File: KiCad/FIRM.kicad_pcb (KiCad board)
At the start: 4 copper layers, 95 parts, among them J1 Conn_01x02_Pin, J3 Micro_SD_Card_Det2, J5 USB_C_Receptacle_USB2.0_16P, Q2 IRLML6402, SW1 PTS815, U1 STM32F405RGTx, U2 MIC5219-3.3YM5, U7 W25Q128JVS, X2 32.768khz, Y1 12mhz

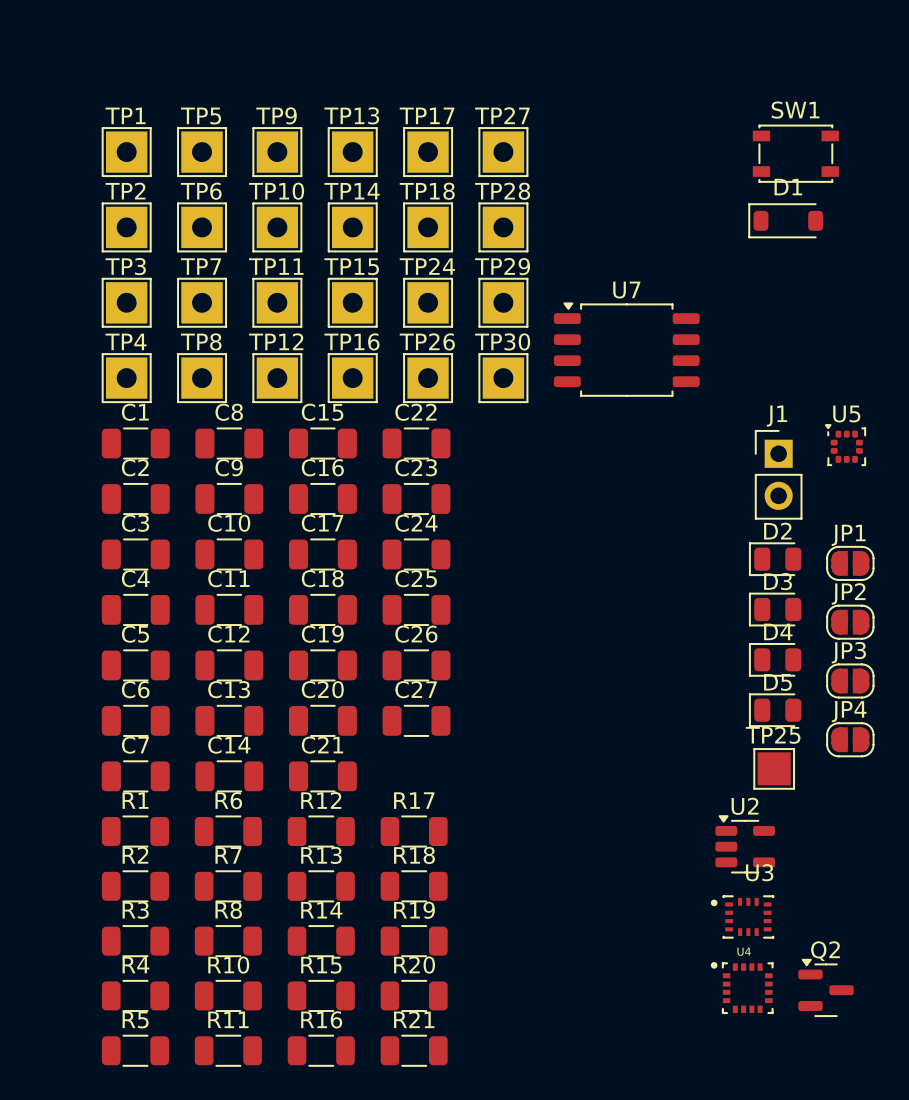
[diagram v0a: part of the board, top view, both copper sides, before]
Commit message: changing some sizes
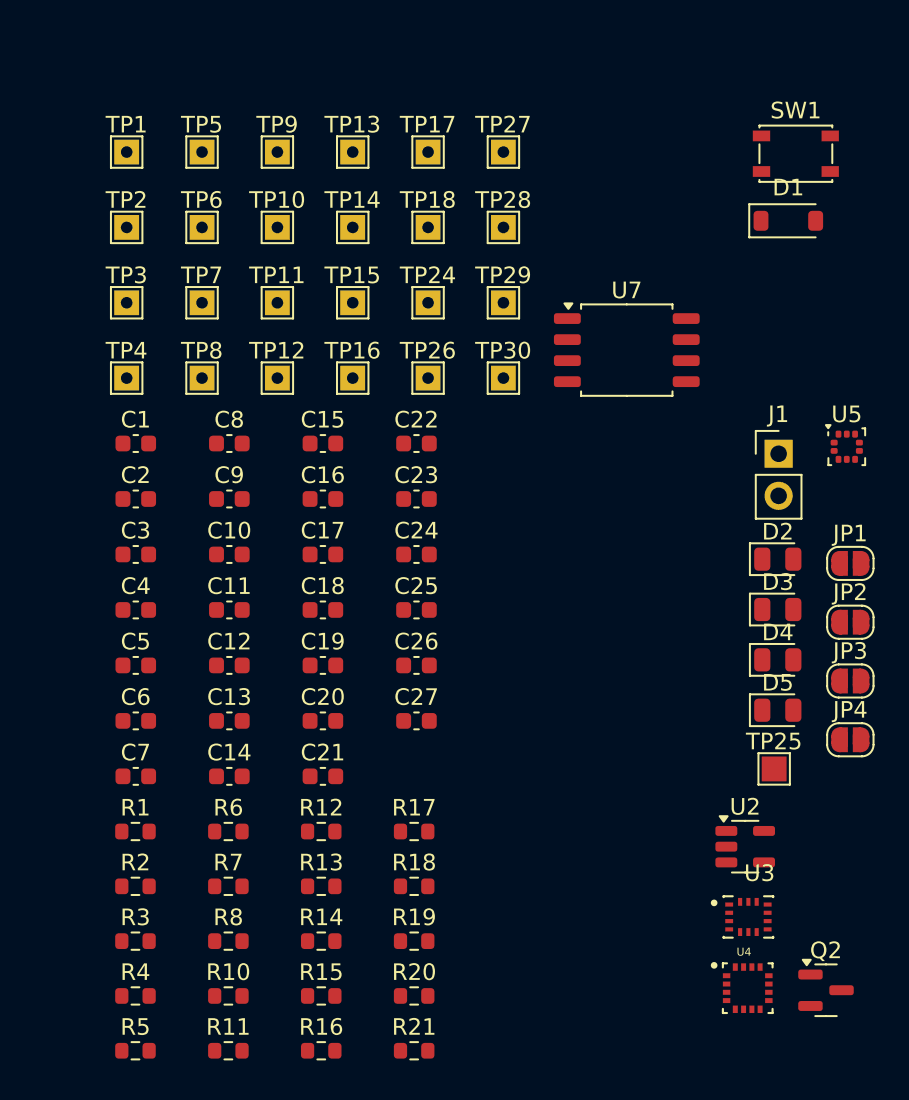
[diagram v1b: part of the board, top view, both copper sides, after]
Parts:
- C1, C10, C11, C12, C13, C14, C15, C16, C17, C18, C19, C2, C20, C21, C22, C23, C24, C25, C26, C27, C3, C4, C5, C6, C7, C8, C9: footprint Capacitor_SMD:C_1206_3216Metric -> Capacitor_SMD:C_0603_1608Metric
- R1, R10, R11, R12, R13, R14, R15, R16, R17, R18, R19, R2, R20, R21, R3, R4, R5, R6, R7, R8: footprint Resistor_SMD:R_1206_3216Metric -> Resistor_SMD:R_0603_1608Metric
- TP1, TP10, TP11, TP12, TP13, TP14, TP15, TP16, TP17, TP18, TP2, TP24, TP26, TP27, TP28, TP29, TP3, TP30, TP4, TP5, TP6, TP7, TP8, TP9: footprint TestPoint:TestPoint_THTPad_2.5x2.5mm_Drill1.2mm -> TestPoint:TestPoint_THTPad_1.5x1.5mm_Drill0.7mm
- TP25: footprint TestPoint:TestPoint_Pad_2.0x2.0mm -> TestPoint:TestPoint_Pad_1.5x1.5mm

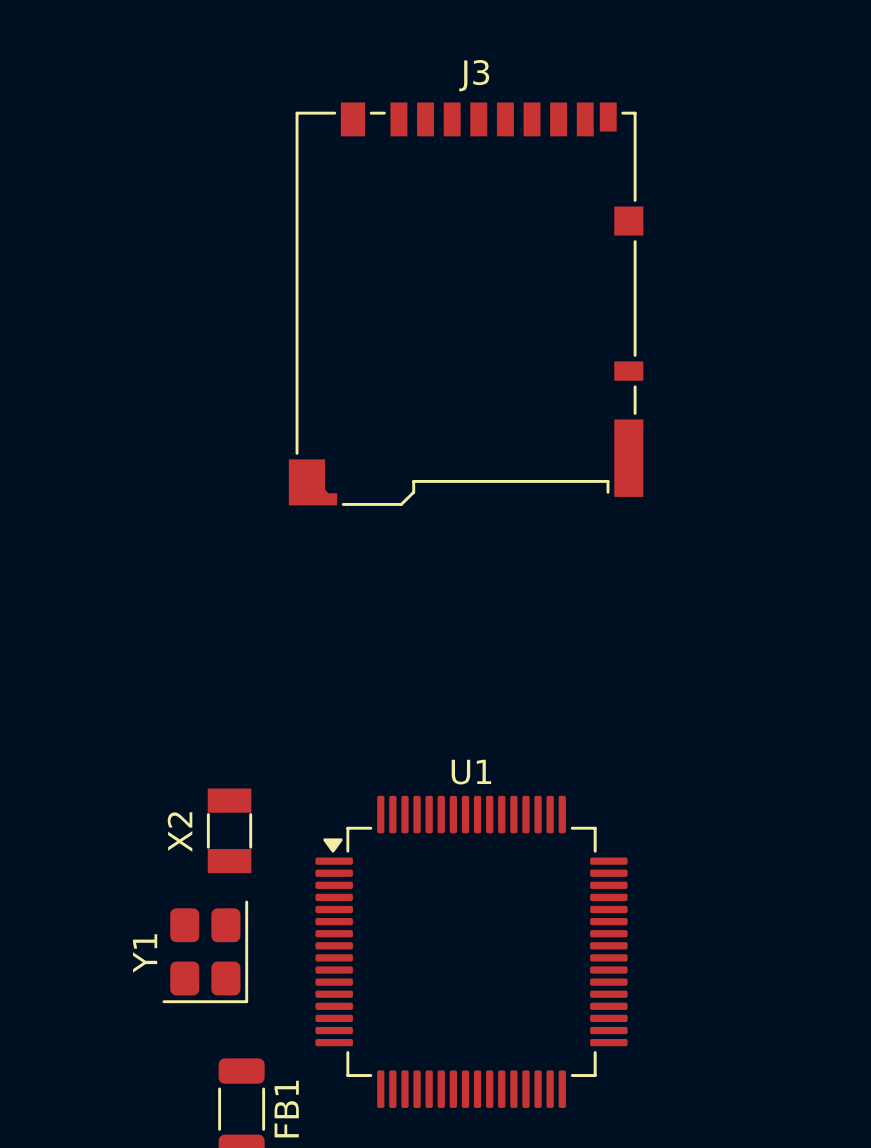
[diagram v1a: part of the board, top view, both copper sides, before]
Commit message: update crystal and sd card port
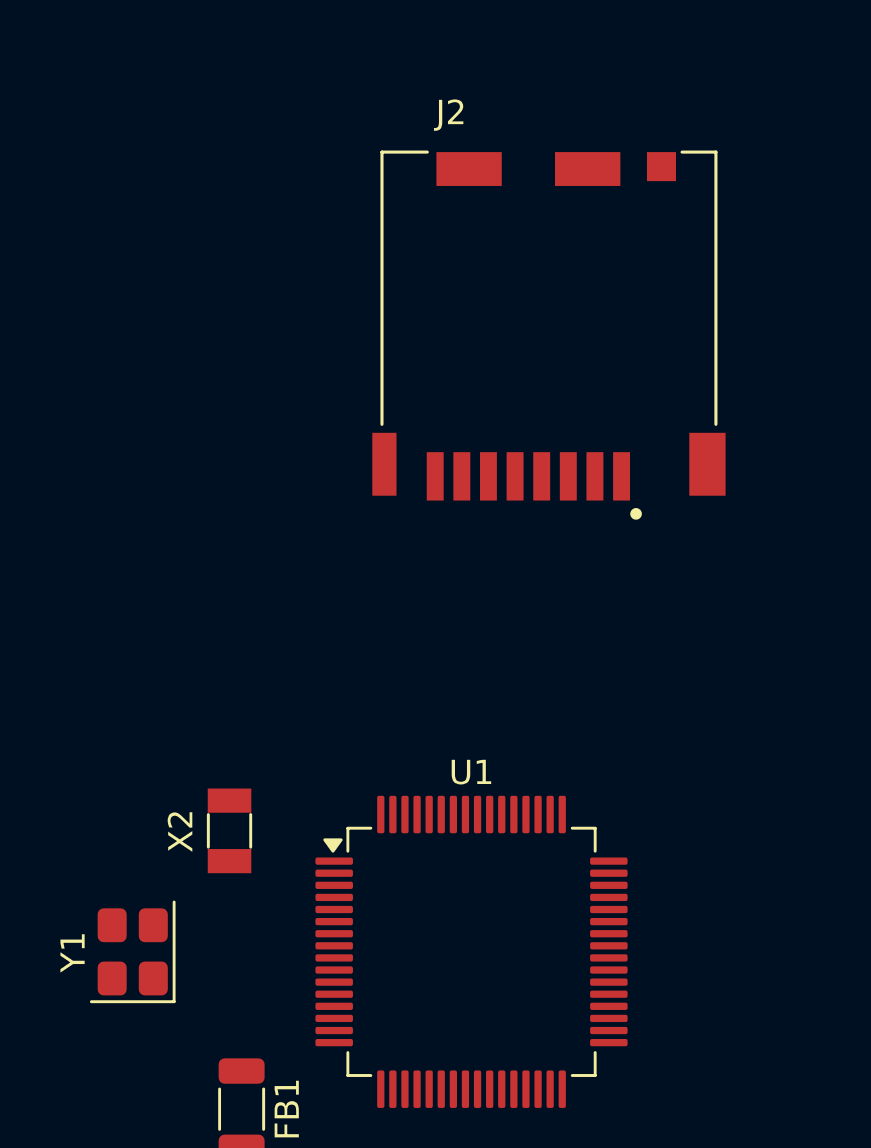
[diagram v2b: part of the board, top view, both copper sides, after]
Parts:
- removed J3: Micro_SD_Card_Det2, Connector_Card:microSD_HC_Hirose_DM3BT-DSF-PEJS
- added J2: DM3CS-SF, DM3CS-SF:HRS_DM3CS-SF, F.Cu at (136.5, 53.5)
- Y1: value 12mhz -> 12 MHz; footprint Crystal:Crystal_SMD_3225-4Pin_3.2x2.5mm -> Crystal:Crystal_SMD_Abracon_ABM8G-4Pin_3.2x2.5mm
- moved Y1 3.00 mm to (119.5, 79.5)
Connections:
- Y1 pad 1: /HSE_OUT -> /HSE_IN
- Y1 pad 2: /HSE_IN -> GND
- Y1 pad 3: (no net) -> /HSE_OUT
- Y1 pad 4: (no net) -> GND

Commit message: rough layout
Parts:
- JP1, JP2, JP3, JP4, U7: moved to B.Cu
- moved J1 99.9 mm to (111.0, 105.5)
- moved U4 97.5 mm to (146.0, 59.5)
- moved TP25 97.1 mm to (132.5, 63.0)
- moved Q2 96.6 mm to (121.0, 107.0), turned to 180 degrees
- moved D5 95.2 mm to (116.5, 104.0), turned to 90 degrees
- moved R5 94.3 mm to (136.3, 50.5), turned to 180 degrees
- moved SW1 93.5 mm to (120.5, 63.5), turned to -90 degrees
- moved JP4 92.0 mm to (151.7, 52.5)
- moved R7 90.7 mm to (135.5, 47.5), turned to 180 degrees
- moved R6 89.2 mm to (117.0, 59.0), turned to -90 degrees
- moved R4 88.9 mm to (136.3, 53.0), turned to 180 degrees
- moved R20 88.9 mm to (136.0, 63.0), turned to -90 degrees
- moved D1 87.1 mm to (126.5, 107.0), turned to -90 degrees
- moved JP3 87.0 mm to (151.7, 56.0)
- moved TP30 86.4 mm to (111.0, 73.8), turned to -90 degrees
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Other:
- board outline added: 57.5 x 70.3 mm

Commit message: Use project library instead of global library
Also reorganize footprints, custom symbols, and 3d models. Updated README about using KiCad in the project.
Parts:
- U3: footprint ICM-45686:IC_ICM-45686 -> sensors:IC_ICM-45686
- U4: footprint MMC5983MA:PQFN50P300X300X100-16N -> sensors:IC_MMC5983MA
- U5: footprint Package_LGA:ST_HLGA-10_2x2mm_P0.5mm_LayoutBorder3x2y -> sensors:BMP581
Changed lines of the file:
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@@
 		(embedded_fonts no)
 	)
-	(footprint "ICM-45686:IC_ICM-45686"
+	(footprint "sensors:IC_ICM-45686"
 		(layer "F.Cu")
 		(at 151.5 99.5)
@@
 		)
 		(embedded_fonts no)
+		(model "${KIPRJMOD}/3dmodels/ICM-45686.step"
+			(offset
+				(xyz 0 0 0)
+			)
+			(scale
+				(xyz 1 1 1)
+			)
+			(rotate
+				(xyz -90 -0 -0)
+			)
+		)
 	)
 	(footprint "TestPoint:TestPoint_THTPad_1.5x1.5mm_Drill0.7mm"
@@
 		)
 	)
-	(footprint "Package_LGA:ST_HLGA-10_2x2mm_P0.5mm_LayoutBorder3x2y"
+	(footprint "sensors:BMP581"
 		(layer "F.Cu")
 		(at 145 93.5)
@@
 		)
 		(embedded_fonts no)
-		(model "${KICAD9_3DMODEL_DIR}/Package_LGA.3dshapes/ST_HLGA-10_2x2mm_P0.5mm_LayoutBorder3x2y.step"
+		(model "${KIPRJMOD}/3dmodels/BMP581.step"
 			(offset
 				(xyz 0 0 0)
@@
 			)
 			(rotate
-				(xyz 0 0 0)
+				(xyz -90 -0 -0)
 			)
 		)
@@
 		)
 	)
-	(footprint "MMC5983MA:PQFN50P300X300X100-16N"
+	(footprint "sensors:IC_MMC5983MA"
 		(layer "F.Cu")
 		(at 146 59.5)
@@
 				(font
 					(size 0.48 0.48)
-					(thickness 0.15)
+					(thickness 0.12)
 				)
 			)
@@
 				(font
 					(size 0.48 0.48)
-					(thickness 0.15)
+					(thickness 0.12)
 				)
 			)
@@
 		)
 		(embedded_fonts no)
+		(model "${KIPRJMOD}/3dmodels/MMC5983MA.step"
+			(offset
+				(xyz 0 0 0)
+			)
+			(scale
+				(xyz 1 1 1)
+			)
+			(rotate
+				(xyz -90 -0 -0)
+			)
+		)
 	)
 	(footprint "Resistor_SMD:R_0603_1608Metric"

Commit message: im firm
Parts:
- removed J5: USB_C_Receptacle_USB2.0_16P, Connector_USB:USB_C_Receptacle_Amphenol_124019772112A
- removed R16, R17: 5.1k, Resistor_SMD:R_0603_1608Metric
- added H1: MountingHole_Pad, MountingHole:MountingHole_3.2mm_M3_Pad_Via, F.Cu at (113.2, 130.5)
- added H2: MountingHole_Pad, MountingHole:MountingHole_3.2mm_M3_Pad_Via, F.Cu at (130.5, 100.0)
- added H3: MountingHole_Pad, MountingHole:MountingHole_3.2mm_M3_Pad_Via, F.Cu at (100.0, 100.0)
- added R22: 5.1k, Resistor_SMD:R_0603_1608Metric, F.Cu at (124.0, 133.2)
- added R9: 5.1k, Resistor_SMD:R_0603_1608Metric, F.Cu at (123.1, 131.6)
- added U6: A-USBC-20F0-EA-GSR05, connectors:A-USBC-20F0-EA-GSR05, F.Cu at (125.0, 125.5)
- J2, TP25: moved to B.Cu
- moved TP27 93.1 mm to (97.5, 127.5)
- moved TP17 88.6 mm to (105.2, 132.6)
- moved TP9 83.4 mm to (102.6, 132.6)
- moved JP2 82.8 mm to (105.0, 128.0), turned to -90 degrees
- moved JP4 82.7 mm to (105.8, 121.2)
- moved JP3 82.2 mm to (105.8, 124.2)
- moved JP1 81.6 mm to (101.5, 128.0), turned to -90 degrees
- moved TP8 77.8 mm to (100.1, 132.6)
- moved U4 76.7 mm to (101.5, 122.0), turned to 90 degrees
- moved TP28 76.5 mm to (97.5, 130.0)
- moved TP5 75.8 mm to (97.5, 119.9)
- moved C18 75.7 mm to (102.1, 124.8), turned to 0 degrees
- moved C17 69.4 mm to (100.7, 118.4), turned to 0 degrees
- moved TP4 67.7 mm to (97.5, 117.3), turned to 90 degrees
- moved TP18 67.2 mm to (107.7, 132.6)
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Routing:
- net GND: track 0.00 -> 60.7 mm, vias 0 -> 55
- net /I2C1_SDA: track 0.00 -> 49.9 mm, vias 0 -> 1
- net /PB4: track 0.00 -> 47.0 mm, vias 0 -> 2
- net /BOOT0: track 0.00 -> 46.8 mm, vias 0 -> 2
- net /I2C1_SCL: track 0.00 -> 45.8 mm, vias 0 -> 5
- net /MOSI2: track 0.00 -> 45.6 mm, vias 0 -> 4
- net VBUS: track 0.00 -> 44.7 mm
- net /PB5: track 0.00 -> 42.8 mm, vias 0 -> 4
- net /MISO2: track 0.00 -> 41.9 mm, vias 0 -> 4
- net Net-(D2-A): track 0.00 -> 41.3 mm, vias 0 -> 4
- net /SDIO_D2: track 0.00 -> 41.0 mm, vias 0 -> 3
- net /SDIO_D1: track 0.00 -> 40.5 mm, vias 0 -> 2
- net /SCK2: track 0.00 -> 40.5 mm, vias 0 -> 3
- net /SDIO_D3: track 0.00 -> 39.4 mm, vias 0 -> 4
- net /SDIO_CMD: track 0.00 -> 39.3 mm, vias 0 -> 6
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- added copper zone on In2.Cu, net +3.3V
- added copper zone on In1.Cu, net GND
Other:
- board size 57.5 x 70.3 mm -> 38.5 x 38.5 mm

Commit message: for the clanker
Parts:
- H1, H2, H3: footprint MountingHole:MountingHole_3.2mm_M3_Pad_Via -> MountingHole:MountingHole_2.2mm_M2_Pad_Via
- moved R6 74.0 mm to (180.2, 108.3), turned to 0 degrees
- moved R8 72.7 mm to (178.2, 125.5), turned to 0 degrees
- moved R5 70.3 mm to (179.7, 110.0), turned to 0 degrees
- moved C23 70.0 mm to (174.2, 121.3)
- moved Q2 68.9 mm to (171.2, 129.8), turned to -90 degrees
- moved R7 68.4 mm to (179.4, 111.5), turned to 180 degrees
- moved C22 68.0 mm to (168.0, 131.0)
- moved U2 67.8 mm to (171.2, 121.0), turned to 90 degrees
- moved C5 67.5 mm to (180.2, 104.5), turned to 0 degrees
- moved D1 66.2 mm to (173.7, 126.0), turned to 0 degrees
- moved D5 65.5 mm to (165.4, 126.3), turned to 0 degrees
- moved C9 64.8 mm to (181.9, 110.8), turned to 90 degrees
- moved C24 63.5 mm to (171.2, 118.0)
- moved R15 60.0 mm to (168.4, 126.0)
- moved C2 56.9 mm to (166.9, 100.0), turned to 0 degrees
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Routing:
- net GND: track 60.7 -> 4.16 mm, vias 55 -> 4
- net /I2C1_SDA: track 49.9 -> 1.83 mm, vias 1 -> 0
- net /PB4: track 47.0 -> 0.00 mm, vias 2 -> 0
- net /BOOT0: track 46.8 -> 0.00 mm, vias 2 -> 0
- net VBUS: track 44.7 -> 0.00 mm
- net /I2C1_SCL: track 45.8 -> 1.71 mm, vias 5 -> 0
- net /MOSI2: track 45.6 -> 2.21 mm, vias 4 -> 0
- net /PB5: track 42.8 -> 0.00 mm, vias 4 -> 0
- net Net-(D2-A): track 41.3 -> 0.00 mm, vias 4 -> 0
- net /SDIO_D2: track 41.0 -> 0.00 mm, vias 3 -> 0
- net /SDIO_D1: track 40.5 -> 0.00 mm, vias 2 -> 0
- net /SDIO_D3: track 39.4 -> 0.00 mm, vias 4 -> 0
- net /SDIO_CMD: track 39.3 -> 0.00 mm, vias 6 -> 0
- net /SCK2: track 40.5 -> 1.62 mm, vias 3 -> 0
- net /SDIO_CK: track 38.8 -> 0.00 mm, vias 3 -> 0
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
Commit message: bom digikey
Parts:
- TP25: moved to F.Cu
- U5: footprint sensors:BMP581 -> Package_LGA:ST_HLGA-10_2x2mm_P0.5mm_LayoutBorder3x2y
- moved R6 77.3 mm to (103.0, 104.5), turned to -90 degrees
- moved R7 73.3 mm to (106.3, 105.9), turned to 90 degrees
- moved R5 71.9 mm to (107.9, 104.4), turned to -90 degrees
- moved R18 71.2 mm to (103.0, 110.4), turned to 90 degrees
- moved R19 68.2 mm to (102.4, 107.2)
- moved C10 67.1 mm to (113.3, 100.0)
- moved R14 59.1 mm to (103.7, 115.9), turned to 90 degrees
- moved C27 58.4 mm to (105.1, 119.6)
- moved C23 58.2 mm to (116.2, 126.2), turned to 180 degrees
- moved C9 57.6 mm to (124.6, 104.5), turned to 0 degrees
- moved FB1 57.4 mm to (110.5, 119.7), turned to 180 degrees
- moved R21 57.4 mm to (105.2, 113.5), turned to 0 degrees
- moved C16 57.3 mm to (109.9, 123.5), turned to 0 degrees
- moved C11 57.2 mm to (104.8, 109.9), turned to 90 degrees
- moved C19 56.6 mm to (119.7, 120.3), turned to 0 degrees
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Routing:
- net /MOSI2: track 2.21 -> 83.3 mm, vias 0 -> 3
- net /MISO2: track 8.19 -> 85.0 mm, vias 2 -> 7
- net /SCK2: track 1.62 -> 74.8 mm, vias 0 -> 5
- net GND: track 4.16 -> 59.6 mm, vias 4 -> 61
- net /PA8: track 0.00 -> 54.1 mm, vias 0 -> 1
- net /PB10: track 0.00 -> 51.6 mm, vias 0 -> 2
- net /MAG_CS: track 8.77 -> 59.1 mm, vias 1 -> 3
- net /PB11: track 0.00 -> 49.0 mm, vias 0 -> 2
- net /MAG_INT: track 8.27 -> 55.5 mm, vias 0 -> 2
- net /NRST: track 0.00 -> 43.9 mm
- net /FLASH_CS: track 0.00 -> 42.4 mm, vias 0 -> 8
- net /BOOT0: track 0.00 -> 40.9 mm, vias 0 -> 4
- net /PA4: track 0.00 -> 38.8 mm, vias 0 -> 2
- net /USB_D+: track 0.00 -> 38.5 mm, vias 0 -> 4
- net /SD_DETECT: track 0.00 -> 38.0 mm, vias 0 -> 5
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- added copper zone on B.Cu, net +3.3V
- added copper zone on F.Cu, net +3.3V

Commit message: almost done?
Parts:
- TP25: moved to B.Cu
- moved H1 33.2 mm to (113.2, 130.5)
- moved H3 33.2 mm to (100.0, 100.0)
- moved R6 29.3 mm to (132.0, 108.2), turned to 0 degrees
- moved D2 28.0 mm to (99.8, 109.0), turned to -90 degrees
- moved SW1 27.8 mm to (105.5, 101.9), turned to -90 degrees
- moved R7 25.6 mm to (131.2, 111.5), turned to 180 degrees
- moved D3 25.5 mm to (102.0, 111.0)
- moved R18 24.5 mm to (125.2, 100.1), turned to 0 degrees
- moved D4 24.5 mm to (102.8, 108.0)
- moved R5 24.0 mm to (131.3, 110.0), turned to 0 degrees
- moved R11 23.2 mm to (105.2, 110.0)
- moved R20 22.9 mm to (100.0, 105.2), turned to -90 degrees
- moved R12 21.7 mm to (106.2, 108.0)
- moved R19 21.0 mm to (122.0, 99.8)
- moved C15 20.3 mm to (105.2, 105.8), turned to 180 degrees
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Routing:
- net +3.3V: track 8.74 -> 59.1 mm, vias 46 -> 27
- net GND: track 59.6 -> 107.1 mm, vias 61 -> 48
- net /MAG_CS: track 59.1 -> 32.7 mm, vias 3 -> 4
- net /SCK2: track 74.8 -> 49.2 mm, vias 5 -> 10
- net /FLASH_CS: track 42.4 -> 16.9 mm, vias 8 -> 2
- net /HSE_IN: track 30.0 -> 5.15 mm
- net /PA2: track 31.2 -> 55.9 mm, vias 1 -> 4
- net /NRST: track 43.9 -> 21.2 mm
- net /USB_D+: track 38.5 -> 16.6 mm, vias 4 -> 2
- net /MAG_INT: track 55.5 -> 35.0 mm
- net /PB10: track 51.6 -> 32.0 mm
- net /USB_D-: track 35.8 -> 16.7 mm, vias 4 -> 2
- net /DBUG_0: track 2.53 -> 20.8 mm, vias 0 -> 2
- net /SD_DETECT: track 38.0 -> 19.8 mm, vias 5 -> 7
- net /PA0: track 26.2 -> 43.3 mm, vias 2 -> 3
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- removed copper zone on B.Cu, net +3.3V
- removed copper zone on F.Cu, net +3.3V
